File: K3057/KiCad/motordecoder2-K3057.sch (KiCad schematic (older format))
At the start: 47 parts, among them P10 PAD, P11 PAD, P21 PAD, P22 PAD, P23 PAD, P24 PAD, P25 PAD, P26 PAD, P27 PAD, P28 PAD, P29 PAD, P30 PAD, P31 PAD, P32 PAD, P7 PAD, P8 PAD, P9 PROG, Q1 DMG6601LVT, Q2 DMG6601LVT, Q3 PMBT3904VS, Q5 2SC4116, Q6 PMBT3906VS, Q8 PMBT3904VS, U2 ATtiny1606-M

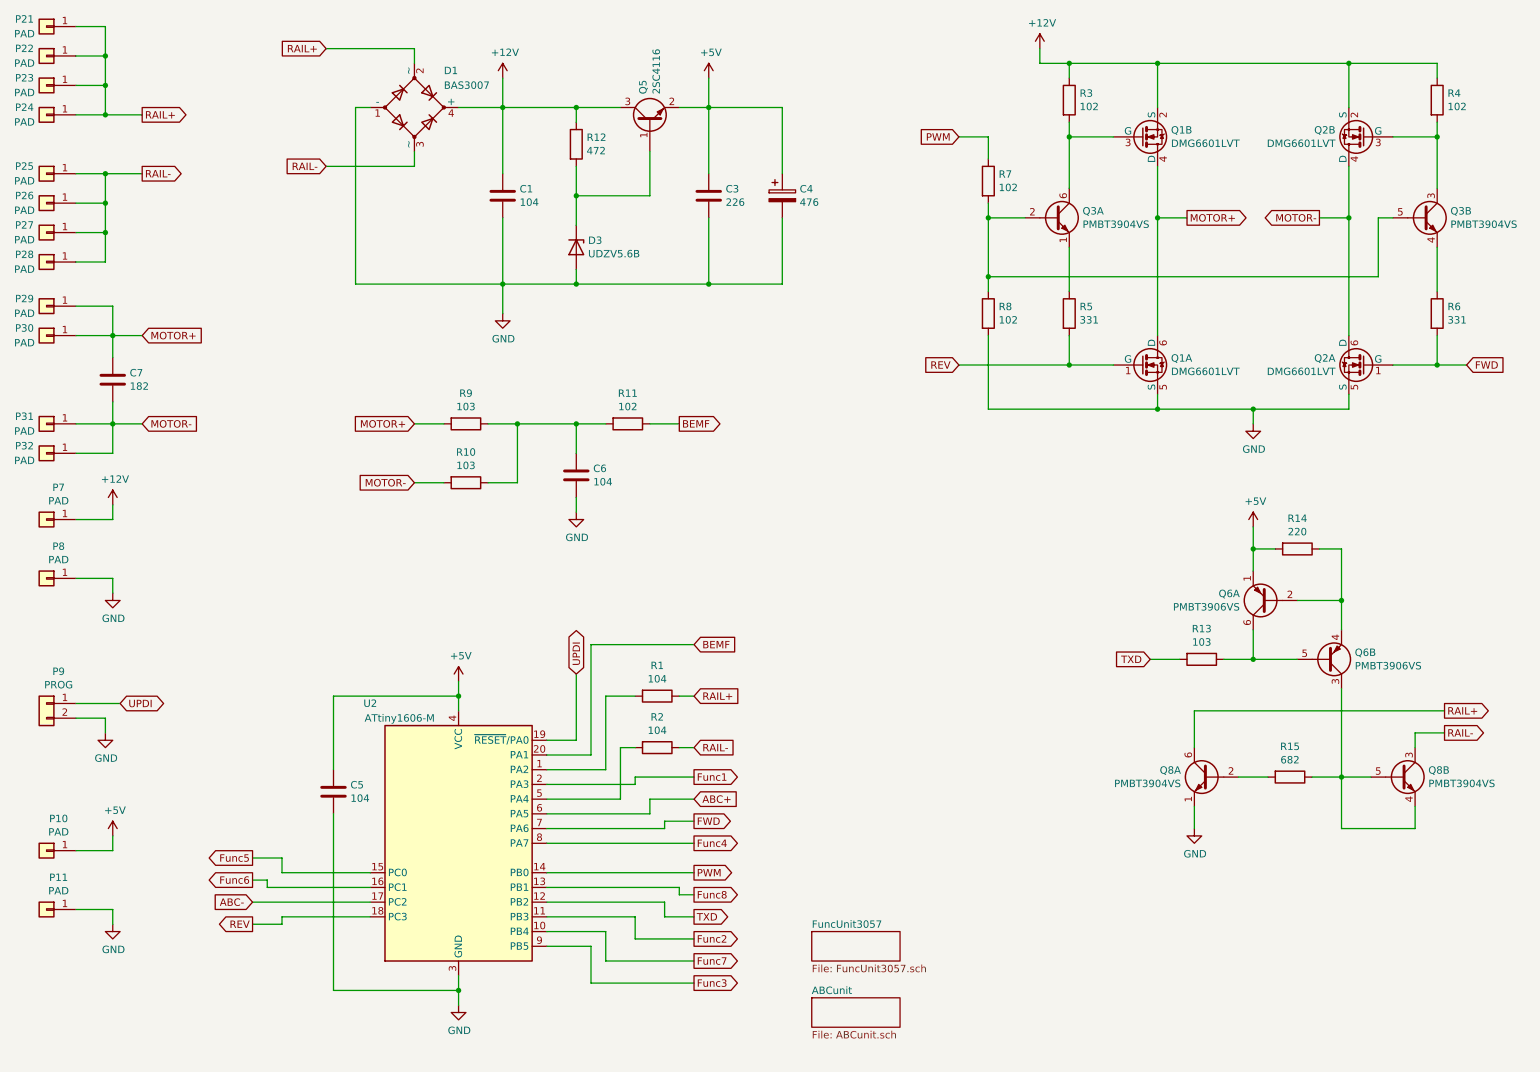
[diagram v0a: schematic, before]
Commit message: 回路の問題点を修正 (K3066: Rev3 / それ以外: Rev2)
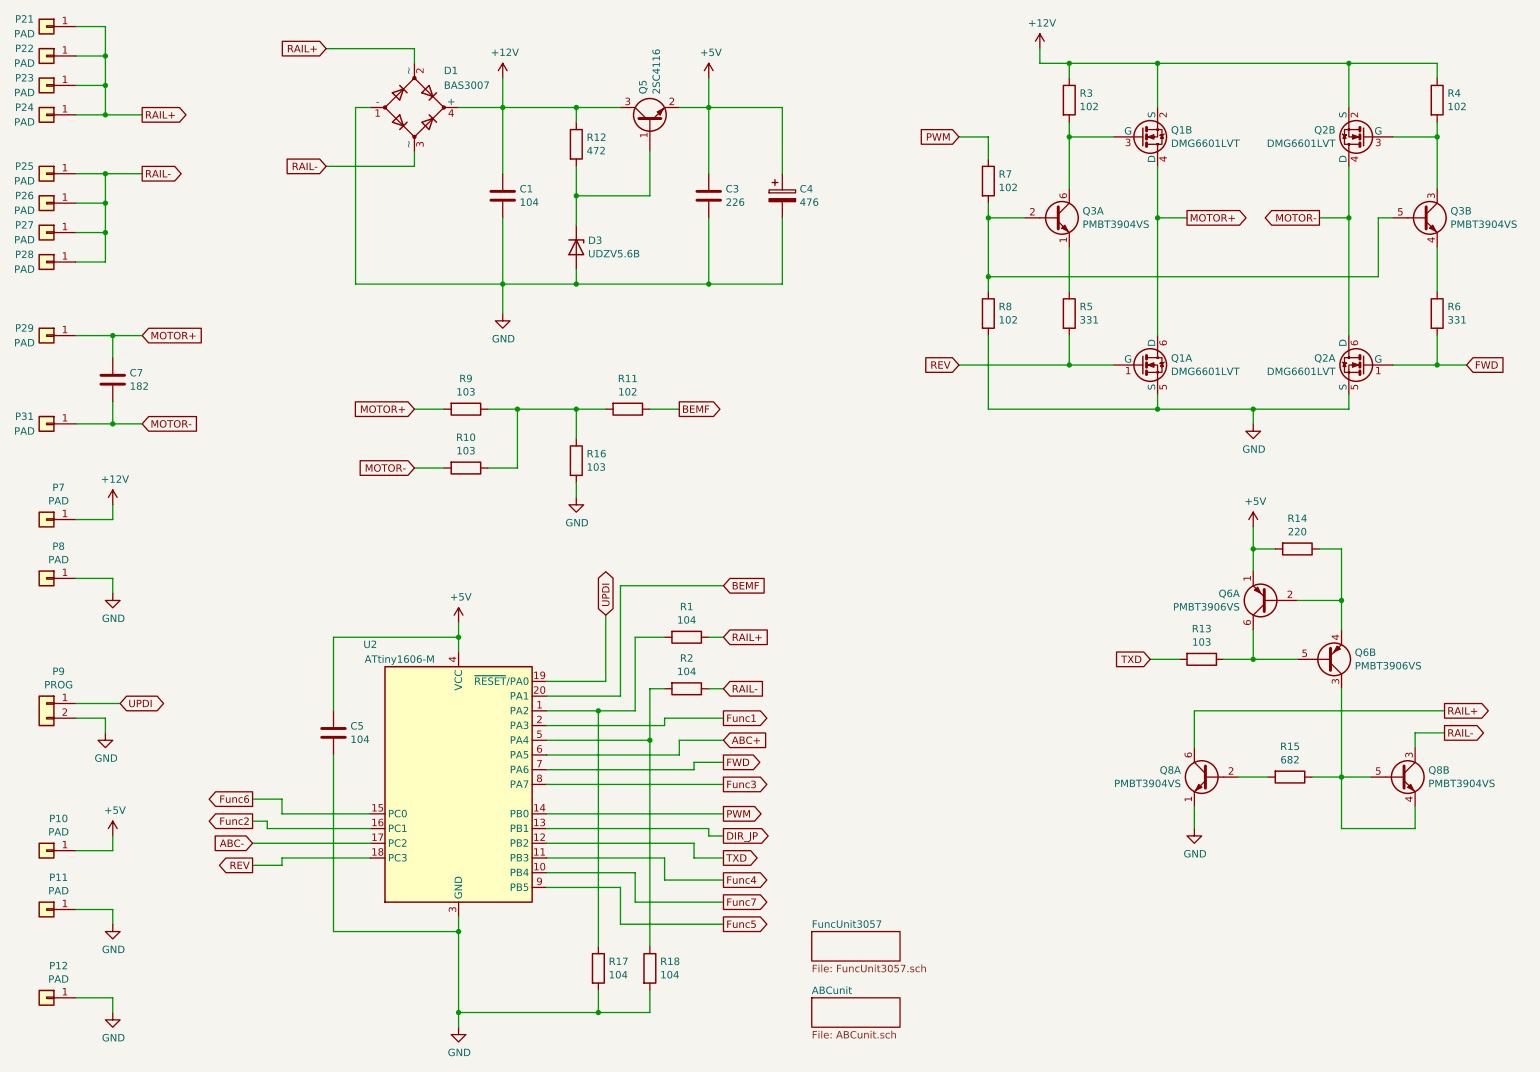
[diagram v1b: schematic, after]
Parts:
- removed C6: 104, footprint:C_1005_v2, symbol Device:C
- removed P30, P32: PAD, footprint:KATO_MOTORPAD_3057_1x2mm, symbol Connector_Generic:Conn_01x01
- added P12: PAD, footprint:PAD_1.0x1.4_SMD, symbol Connector_Generic:Conn_01x01
- added R16: 103, footprint:R_1005, symbol Device:R
- added R17, R18: 104, footprint:R_1005, symbol Device:R
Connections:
- net Func2: now also U2.16 (PC1); no longer U2.11 (PB3)
- net Func3: now also U2.8 (PA7); no longer U2.9 (PB5)
- net Func4: now also U2.11 (PB3); no longer U2.8 (PA7)
- net Func5: now also U2.9 (PB5); no longer U2.15 (PC0)
- net Func6: now also U2.15 (PC0); no longer U2.16 (PC1)
- net GND: now also P12.1 (Pin_1), R16.2, R17.2, R18.2
- net at R10.1, R11.2, R9.1: now also R16.1
- net at R1.2, U2.1 (PA2): now also R17.1
- net at R2.2, U2.5 (PA4): now also R18.1
- net Func8 renamed DIR_JP
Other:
- moved on the sheet: C5, P29, R1, R10, R11, R2, R9, U2
